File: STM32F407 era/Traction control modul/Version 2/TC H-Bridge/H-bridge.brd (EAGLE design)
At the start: 57.8 x 40.3 mm, 30 parts, among them IC5 REG1117, Q5 IRFR3707ZR, Q8 IRFR3707ZR, X5 5566-10

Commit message: more layout work done with added verison for seperate PCB box housing
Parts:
- removed C1: 330n, microbuilder:_0603
- removed Q2: (no value), microbuilder:SOT23-WIDE
- removed R3: 1k5, microbuilder:_0603
- removed R4: 10k, microbuilder:_0603
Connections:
- removed net N$10: Q2.1, U$28.9
- removed net N$12: Q2.2, R3.1, R4.2
- net 3.3V: no longer Q2.3
- net CS: no longer C1.1, R4.1
- net GND: no longer C1.2, R3.2
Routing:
- net N$10: track 24.4 -> 0.00 mm, vias 2 -> 0
- net N$12: track 6.10 -> 0.00 mm
- net 3.3V: track 37.1 -> 33.0 mm
- net CS: track 24.6 -> 21.8 mm
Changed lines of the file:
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@@
 <element name="R1" library="microbuilder" package="_0603" value="1k" x="104.4575" y="46.99"/>
 <element name="R2" library="microbuilder" package="_0603" value="1k" x="111.76" y="46.0375" rot="R180"/>
-<element name="Q2" library="microbuilder" package="SOT23-WIDE" value="" x="126.0475" y="19.05" rot="R270"/>
-<element name="R3" library="microbuilder" package="_0603" value="1k5" x="122.2375" y="18.0975" rot="R180"/>
-<element name="R4" library="microbuilder" package="_0603" value="10k" x="129.8575" y="18.0975" rot="R180"/>
-<element name="C1" library="microbuilder" package="_0603" value="330n" x="133.0325" y="18.0975"/>
 </elements>
 <signals>
@@
 <contactref element="C17" pad="1"/>
 <contactref element="Q1" pad="2"/>
-<contactref element="R3" pad="2"/>
-<contactref element="C1" pad="2"/>
 <via x="141.605" y="28.2575" extent="1-16" drill="0.381"/>
 <via x="120.015" y="18.0975" extent="1-16" drill="0.381"/>
@@
 <wire x1="142.5575" y1="24.13" x2="147.0025" y2="19.685" width="0.3048" layer="1"/>
 <wire x1="143.5703" y1="28.84" x2="142.5575" y2="28.84" width="0.3048" layer="1"/>
-<contactref element="Q2" pad="3"/>
 <wire x1="137.795" y1="25.0825" x2="138.43" y2="25.0825" width="0.3048" layer="1"/>
 <wire x1="138.43" y1="25.0825" x2="142.5575" y2="25.0825" width="0.3048" layer="1"/>
-<wire x1="127.0475" y1="19.05" x2="131.1275" y2="19.05" width="0.3048" layer="1"/>
 <wire x1="131.1275" y1="19.05" x2="134.62" y2="22.5425" width="0.3048" layer="1"/>
 <wire x1="134.62" y1="22.5425" x2="134.62" y2="24.4475" width="0.3048" layer="1"/>
@@
 <wire x1="105.2195" y1="46.99" x2="106.95" y2="46.99" width="0.6096" layer="1"/>
 </signal>
-<signal name="N$10">
-<contactref element="U$28" pad="9"/>
-<contactref element="Q2" pad="1"/>
-<wire x1="125.0475" y1="20" x2="128.585" y2="20" width="0.3048" layer="1"/>
-<wire x1="128.585" y1="20" x2="128.5875" y2="20.0025" width="0.3048" layer="1"/>
-<via x="128.5875" y="20.0025" extent="1-16" drill="0.381"/>
-<wire x1="128.5875" y1="20.0025" x2="132.08" y2="20.0025" width="0.3048" layer="16"/>
-<wire x1="132.08" y1="20.0025" x2="134.9375" y2="22.86" width="0.3048" layer="16"/>
-<wire x1="134.9375" y1="22.86" x2="134.9375" y2="24.765" width="0.3048" layer="16"/>
-<wire x1="134.9375" y1="24.765" x2="134.62" y2="25.0825" width="0.3048" layer="16"/>
-<wire x1="134.62" y1="25.0825" x2="131.1275" y2="25.0825" width="0.3048" layer="16"/>
-<wire x1="131.1275" y1="25.0825" x2="130.81" y2="25.4" width="0.3048" layer="16"/>
-<wire x1="130.81" y1="25.4" x2="130.81" y2="30.7975" width="0.3048" layer="16"/>
-<wire x1="130.81" y1="30.7975" x2="131.1275" y2="31.115" width="0.3048" layer="16"/>
-<via x="131.1275" y="31.115" extent="1-16" drill="0.381"/>
-<wire x1="131.1275" y1="31.115" x2="132.2425" y2="31.115" width="0.3048" layer="1"/>
-<wire x1="132.2425" y1="31.115" x2="132.29" y2="31.1625" width="0.3048" layer="1"/>
-</signal>
-<signal name="N$12">
-<contactref element="Q2" pad="2"/>
-<contactref element="R3" pad="1"/>
-<contactref element="R4" pad="2"/>
-<wire x1="122.9995" y1="18.0975" x2="125.045" y2="18.0975" width="0.3048" layer="1"/>
-<wire x1="125.045" y1="18.0975" x2="125.0475" y2="18.1" width="0.3048" layer="1"/>
-<wire x1="125.0475" y1="18.1" x2="129.093" y2="18.1" width="0.3048" layer="1"/>
-<wire x1="129.093" y1="18.1" x2="129.0955" y2="18.0975" width="0.3048" layer="1"/>
-</signal>
 <signal name="CS">
-<contactref element="R4" pad="1"/>
-<contactref element="C1" pad="1"/>
 <contactref element="U$1" pad="7"/>
-<wire x1="130.6195" y1="18.0975" x2="132.2705" y2="18.0975" width="0.3048" layer="1"/>
 <wire x1="136.525" y1="24.4475" x2="147.0025" y2="34.925" width="0.3048" layer="16"/>
-<wire x1="132.2705" y1="18.0975" x2="132.2705" y2="19.2405" width="0.3048" layer="1"/>
 <wire x1="132.2705" y1="19.2405" x2="135.89" y2="22.86" width="0.3048" layer="1"/>
 <wire x1="135.89" y1="22.86" x2="135.89" y2="23.495" width="0.3048" layer="1"/>

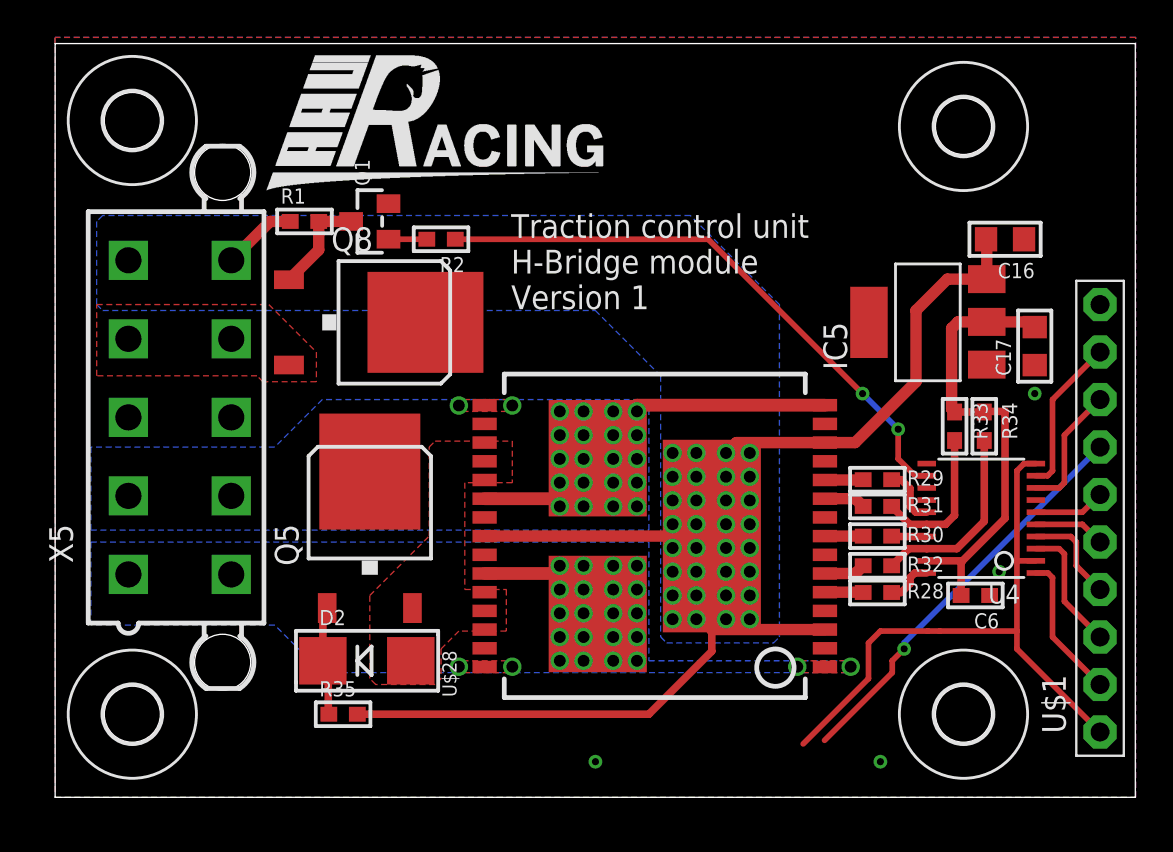
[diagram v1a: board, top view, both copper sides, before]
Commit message: changed H-Bridge design for modular mount, more layout on TC
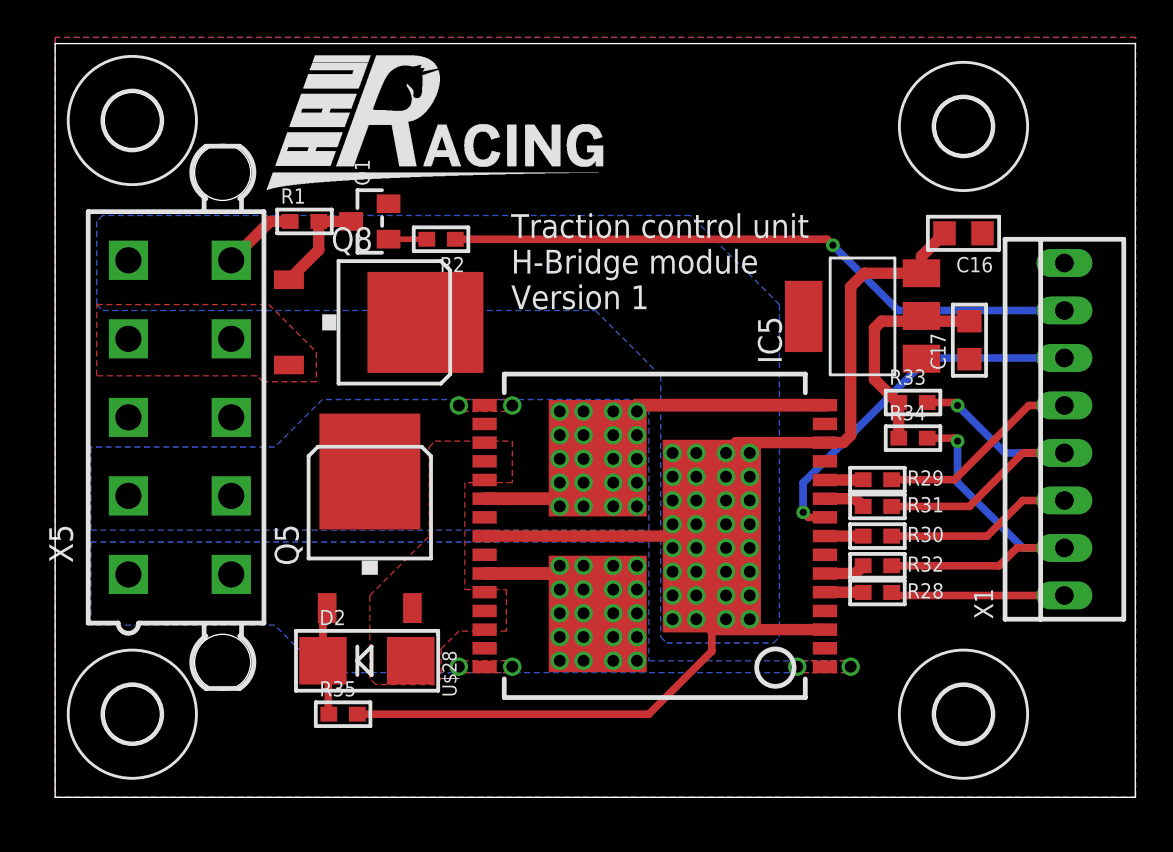
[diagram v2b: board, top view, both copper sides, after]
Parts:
- removed C6: 100n, microbuilder:_0603
- removed U$1: PINHD-1X10, adafruit:1X10-BIG
- removed U4: (no value), adafruit:TSSOP20
- added X1: 22-23-2081, con-molex:22-23-2081
- moved R34 3.86 mm to (137.0, 35.4), turned to 0 degrees
- moved C17 3.51 mm to (140.0, 40.6)
- moved IC5 3.51 mm to (134.3, 41.9)
- moved R33 2.56 mm to (137.0, 37.3), turned to 0 degrees
- moved C16 2.25 mm to (139.7, 46.4)
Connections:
- removed net 3.3V: U$1.1, U4.10, U4.2
- removed net N$1: U$1.2, U4.1
- removed net N$2: U$1.3, U4.3
- removed net N$3: U$1.4, U4.4
- removed net N$4: U$1.5, U4.5
- removed net N$5: U$1.6, U4.6
- removed net N$7: U$1.8, U4.8
- removed net N$8: U$1.9, U4.9
- net 5.0V: no longer C6.2, U4.19
- net CS: now also U$28.9, X1.6; no longer U$1.7
- net EN1H: now also X1.2; no longer U4.18
- net EN2H: now also X1.4; no longer U4.16
- net GND: now also X1.8; no longer C6.1, U$1.10, U4.11
- net MD: now also X1.7; no longer U4.12
- net N$71: now also X1.1; no longer U4.20
- net N$72: now also X1.5; no longer U4.15
- net N$73: now also X1.3; no longer U4.17
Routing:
- net 3.3V: track 33.0 -> 0.00 mm
- net 5.0V: track 24.7 -> 12.1 mm
- net EN2H: track 7.96 -> 18.9 mm, vias 0 -> 1
- net EN1H: track 10.3 -> 20.7 mm, vias 0 -> 1
- net N$8: track 8.40 -> 0.00 mm
- net N$73: track 1.90 -> 10.1 mm
- net N$1: track 7.76 -> 0.00 mm
- net N$72: track 3.15 -> 10.9 mm
- net N$7: track 6.88 -> 0.00 mm
- net N$2: track 6.88 -> 0.00 mm
- net N$71: track 2.49 -> 9.31 mm
- net N$3: track 5.35 -> 0.00 mm
- net N$4: track 3.82 -> 0.00 mm
- net N$5: track 3.82 -> 0.00 mm
- net MD: track 31.4 -> 34.2 mm, vias 2 -> 1
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
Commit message: continued work with last additions
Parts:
- added C1: 1000u, microbuilder:CELEC_3.5MM_10MM
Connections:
- net 12V: now also C1.+
- net GND: now also C1.-
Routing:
- net MD: track 34.2 -> 35.7 mm
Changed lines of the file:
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@@
 <attribute name="OC_FARNELL" value="1756826" x="145.0975" y="35.8775" size="1.778" layer="27" rot="R90" display="off"/>
 </element>
+<element name="C1" library="microbuilder" package="CELEC_3.5MM_10MM" value="1000u" x="123.5075" y="47.625" rot="R90"/>
 </elements>
 <signals>
@@
 <contactref element="Q1" pad="2"/>
 <contactref element="X1" pad="8"/>
+<contactref element="C1" pad="-"/>
 </signal>
 <signal name="5.0V">
@@
 <wire x1="138.684" y1="46.355" x2="137.4521" y2="45.1231" width="0.6096" layer="1"/>
 <wire x1="137.4521" y1="45.1231" x2="137.4521" y2="44.2214" width="0.6096" layer="1"/>
+<contactref element="C1" pad="+"/>
 </signal>
 <signal name="MD">
 <contactref element="R2" pad="1"/>
 <contactref element="X1" pad="7"/>
-<wire x1="112.522" y1="46.0375" x2="132.3975" y2="46.0375" width="0.4064" layer="1"/>
-<wire x1="132.3975" y1="46.0375" x2="132.715" y2="45.72" width="0.4064" layer="1"/>
 <via x="132.715" y="45.72" extent="1-16" drill="0.381"/>
 <wire x1="132.715" y1="45.72" x2="136.2075" y2="42.2275" width="0.4064" layer="16"/>
 <wire x1="136.2075" y1="42.2275" x2="145.0975" y2="42.2275" width="0.4064" layer="16"/>
+<wire x1="112.522" y1="46.0375" x2="120.015" y2="46.0375" width="0.4064" layer="1"/>
+<wire x1="120.015" y1="46.0375" x2="122.2375" y2="43.815" width="0.4064" layer="1"/>
+<wire x1="122.2375" y1="43.815" x2="125.095" y2="43.815" width="0.4064" layer="1"/>
+<wire x1="125.095" y1="43.815" x2="127" y2="45.72" width="0.4064" layer="1"/>
+<wire x1="127" y1="45.72" x2="132.715" y2="45.72" width="0.4064" layer="1"/>
 </signal>
 <signal name="N$9">
@@
 </signal>
 </signals>
-<errors>
-</errors>
 </board>
 </drawing>
